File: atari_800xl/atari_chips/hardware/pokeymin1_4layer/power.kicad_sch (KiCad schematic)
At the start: 10 parts

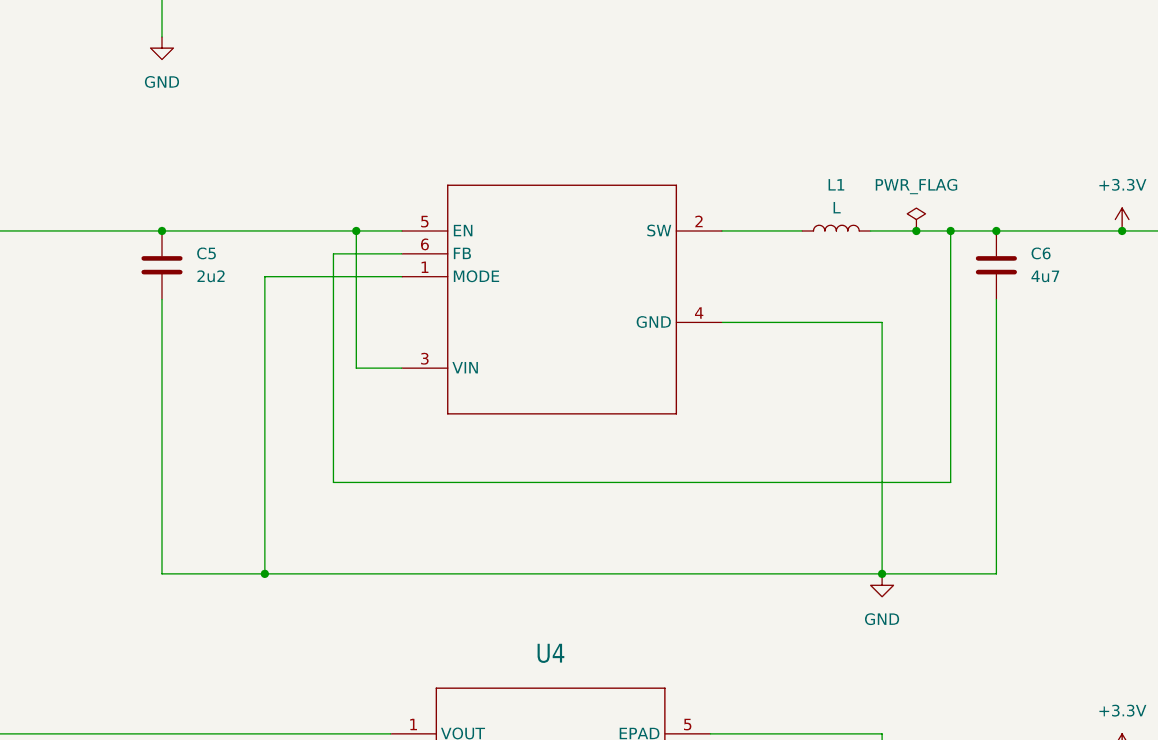
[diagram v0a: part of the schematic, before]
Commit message: Change regulator to a linear one that works with the io pin protection scheme
git-svn-id: svn+ssh://192.168.0.3/home/svnfpga/repo/trunk@1479 d6161ac3-aae1-4d52-9b05-ea9ac36b53d3
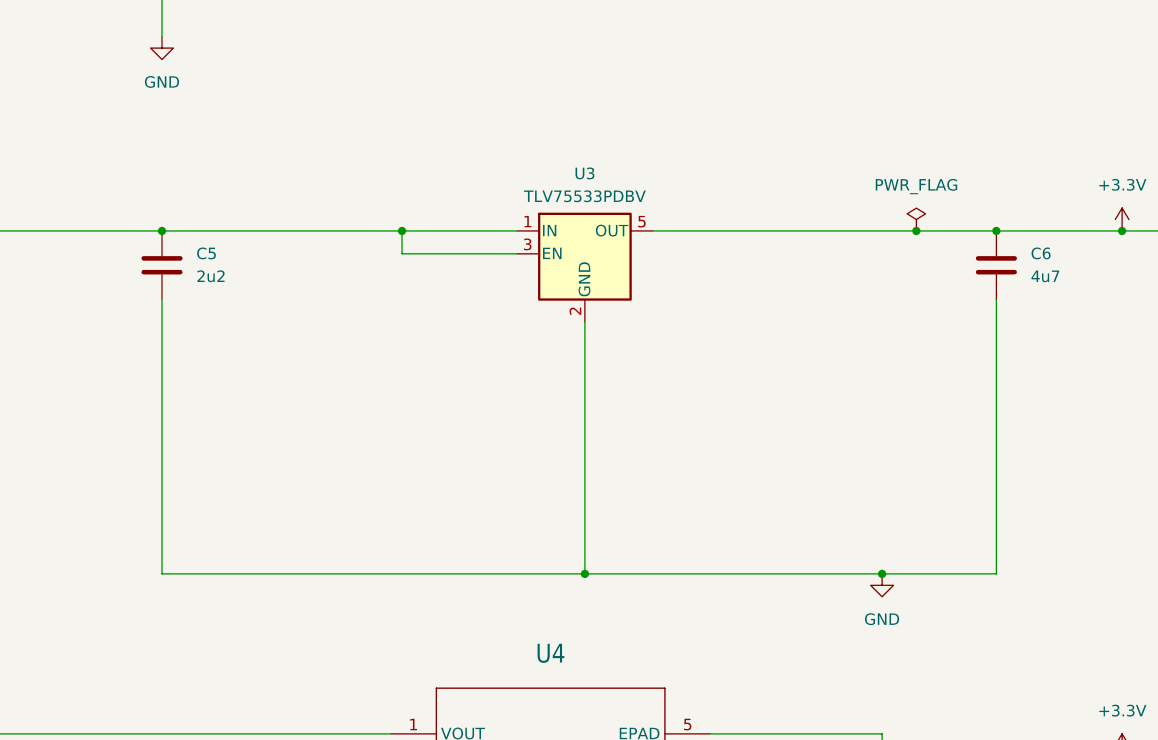
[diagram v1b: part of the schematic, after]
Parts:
- removed L1: L, Inductor_SMD:L_1008_2520Metric_Pad1.43x2.20mm_HandSolder, symbol Device:L
- removed U3: ~, max10:DRY6, symbol max10u169:TPS62237DRYR
- added U3: TLV75533PDBV, Package_TO_SOT_SMD:SOT-23-5, symbol Regulator_Linear:TLV75533PDBV
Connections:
- net +3.3V: now also U3.5 (OUT)
- net +5V: now also U3.1 (IN), U3.3 (EN)
- net GND: now also U3.2 (GND)
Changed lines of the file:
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@@
 	(paper "A4")
+	(junction
+		(at 83.82 60.96)
+		(diameter 0)
+		(color 0 0 0 0)
+	)
 	(junction
 		(at 57.15 60.96)
@@
 	)
 	(junction
-		(at 68.58 99.06)
-		(diameter 0)
-		(color 0 0 0 0)
-	)
-	(junction
 		(at 50.8 31.75)
 		(diameter 0)
@@
 	)
 	(junction
-		(at 144.78 60.96)
-		(diameter 0)
-		(color 0 0 0 0)
-	)
-	(junction
 		(at 62.23 31.75)
 		(diameter 0)
@@
 	)
 	(junction
-		(at 78.74 60.96)
+		(at 104.14 99.06)
 		(diameter 0)
 		(color 0 0 0 0)
@@
 	(wire
 		(pts
-			(xy 78.74 76.2) (xy 78.74 60.96)
-		)
-		(stroke
-			(width 0)
-			(type default)
-		)
-	)
-	(wire
-		(pts
-			(xy 137.16 99.06) (xy 137.16 71.12)
-		)
-		(stroke
-			(width 0)
-			(type default)
-		)
-	)
-	(wire
-		(pts
 			(xy 50.8 31.75) (xy 57.15 31.75)
 		)
@@
 	(wire
 		(pts
-			(xy 140.97 60.96) (xy 144.78 60.96)
+			(xy 140.97 60.96) (xy 149.86 60.96)
 		)
 		(stroke
@@
 	(wire
 		(pts
-			(xy 76.2 63.5) (xy 83.82 63.5)
-		)
-		(stroke
-			(width 0)
-			(type default)
-		)
-	)
-	(wire
-		(pts
-			(xy 68.58 66.04) (xy 68.58 99.06)
-		)
-		(stroke
-			(width 0)
-			(type default)
-		)
-	)
-	(wire
-		(pts
 			(xy 57.15 68.58) (xy 57.15 99.06)
 		)
@@
 	(wire
 		(pts
-			(xy 83.82 66.04) (xy 68.58 66.04)
+			(xy 96.52 63.5) (xy 83.82 63.5)
+		)
+		(stroke
+			(width 0)
+			(type default)
+		)
+	)
+	(wire
+		(pts
+			(xy 111.76 60.96) (xy 140.97 60.96)
 		)
 		(stroke
@@
 	(wire
 		(pts
-			(xy 135.89 60.96) (xy 140.97 60.96)
-		)
-		(stroke
-			(width 0)
-			(type default)
-		)
-	)
-	(wire
-		(pts
-			(xy 83.82 76.2) (xy 78.74 76.2)
-		)
-		(stroke
-			(width 0)
-			(type default)
-		)
-	)
-	(wire
-		(pts
 			(xy 118.11 121.92) (xy 123.19 121.92)
 		)
@@
 	(wire
 		(pts
-			(xy 119.38 60.96) (xy 128.27 60.96)
+			(xy 104.14 71.12) (xy 104.14 99.06)
 		)
 		(stroke
@@
 	(wire
 		(pts
-			(xy 78.74 60.96) (xy 83.82 60.96)
-		)
-		(stroke
-			(width 0)
-			(type default)
-		)
-	)
-	(wire
-		(pts
 			(xy 34.29 60.96) (xy 57.15 60.96)
 		)
@@
 	(wire
 		(pts
+			(xy 104.14 99.06) (xy 137.16 99.06)
+		)
+		(stroke
+			(width 0)
+			(type default)
+		)
+	)
+	(wire
+		(pts
 			(xy 123.19 121.92) (xy 123.19 119.38)
 		)
@@
 	(wire
 		(pts
+			(xy 83.82 60.96) (xy 96.52 60.96)
+		)
+		(stroke
+			(width 0)
+			(type default)
+		)
+	)
+	(wire
+		(pts
 			(xy 149.86 68.58) (xy 149.86 99.06)
 		)
@@
 	(wire
 		(pts
-			(xy 144.78 60.96) (xy 149.86 60.96)
-		)
-		(stroke
-			(width 0)
-			(type default)
-		)
-	)
-	(wire
-		(pts
 			(xy 62.23 21.59) (xy 62.23 24.13)
 		)
@@
 	(wire
 		(pts
-			(xy 144.78 88.9) (xy 76.2 88.9)
-		)
-		(stroke
-			(width 0)
-			(type default)
-		)
-	)
-	(wire
-		(pts
-			(xy 76.2 88.9) (xy 76.2 63.5)
+			(xy 83.82 63.5) (xy 83.82 60.96)
 		)
 		(stroke
@@
 	(wire
 		(pts
-			(xy 68.58 99.06) (xy 137.16 99.06)
+			(xy 57.15 99.06) (xy 104.14 99.06)
 		)
 		(stroke
@@
 	(wire
 		(pts
-			(xy 144.78 60.96) (xy 144.78 88.9)
-		)
-		(stroke
-			(width 0)
-			(type default)
-		)
-	)
-	(wire
-		(pts
-			(xy 57.15 99.06) (xy 68.58 99.06)
-		)
-		(stroke
-			(width 0)
-			(type default)
-		)
-	)
-	(wire
-		(pts
 			(xy 57.15 31.75) (xy 57.15 39.37)
 		)
@@
 	(wire
 		(pts
-			(xy 57.15 60.96) (xy 78.74 60.96)
-		)
-		(stroke
-			(width 0)
-			(type default)
-		)
-	)
-	(wire
-		(pts
-			(xy 137.16 71.12) (xy 119.38 71.12)
+			(xy 57.15 60.96) (xy 83.82 60.96)
 		)
 		(stroke
@@
 	)
 	(symbol
+		(lib_id "Regulator_Linear:TLV75533PDBV")
+		(at 104.14 63.5 0)
+		(unit 1)
+		(exclude_from_sim no)
+		(in_bom yes)
+		(on_board yes)
+		(dnp no)
+		(fields_autoplaced yes)
+		(property "Reference" "U3"
+			(at 104.14 54.61 0)
+			(effects
+				(font
+					(size 1.27 1.27)
+				)
+			)
+		)
+		(property "Value" "TLV75533PDBV"
+			(at 104.14 57.15 0)
+			(effects
+				(font
+					(size 1.27 1.27)
+				)
+			)
+		)
+		(property "Footprint" "Package_TO_SOT_SMD:SOT-23-5"
+			(at 104.14 55.245 0)
+			(effects
+				(font
+					(size 1.27 1.27)
+					(italic yes)
+				)
+				(hide yes)
+			)
+		)
+		(property "Datasheet" "http://www.ti.com/lit/ds/symlink/tlv755p.pdf"
+			(at 104.14 62.23 0)
+			(effects
+				(font
+					(size 1.27 1.27)
+				)
+				(hide yes)
+			)
+		)
+		(property "Description" "500mA Low Dropout Voltage Regulator, Fixed Output 3.3V, SOT-23-5"
+			(at 104.14 63.5 0)
+			(effects
+				(font
+					(size 1.27 1.27)
+				)
+				(hide yes)
+			)
+		)
+		(pin "5"
+		)
+		(pin "4"
+		)
+		(pin "1"
+		)
+		(pin "3"
+		)
+		(pin "2"
+		)
+		(instances
+			(project ""
+				(path "/f8f92944-710a-49a0-a698-f840e5f20e15/b3c63cf3-5aec-4ac7-b511-941f39b58d95"
+					(reference "U3")
+					(unit 1)
+				)
+			)
+		)
+	)
+	(symbol
 		(lib_id "power:PWR_FLAG")
 		(at 140.97 60.96 0)
@@
 					(unit 1)
 				)
-			)
-		)
-	)
-	(symbol
-		(lib_id "Device:L")
-		(at 132.08 60.96 90)
-		(unit 1)
-		(exclude_from_sim no)
-		(in_bom yes)
-		(on_board yes)
-		(dnp no)
-		(fields_autoplaced yes)
-		(property "Reference" "L1"
-			(at 132.08 55.88 90)
-			(effects
-				(font
-					(size 1.27 1.27)
-				)
-			)
-		)
-		(property "Value" "L"
-			(at 132.08 58.42 90)
-			(effects
-				(font
-					(size 1.27 1.27)
-				)
-			)
-		)
-		(property "Footprint" "Inductor_SMD:L_1008_2520Metric_Pad1.43x2.20mm_HandSolder"
-			(at 132.08 60.96 0)
-			(effects
-				(font
-					(size 1.27 1.27)
-				)
-				(hide yes)
-			)
-		)
-		(property "Datasheet" "~"
-			(at 132.08 60.96 0)
-			(effects
-				(font
-					(size 1.27 1.27)
-				)
-				(hide yes)
-			)
-		)
-		(property "Description" "Inductor"
-			(at 132.08 60.96 0)
-			(effects
-				(font
-					(size 1.27 1.27)
-				)
-				(hide yes)
-			)
-		)
-		(pin "2"
-		)
-		(pin "1"
-		)
-		(instances
-			(project ""
-				(path "/f8f92944-710a-49a0-a698-f840e5f20e15/b3c63cf3-5aec-4ac7-b511-941f39b58d95"
-					(reference "L1")
-					(unit 1)
-				)
-			)
-		)
-	)
-	(symbol
-		(lib_id "max10u169:TPS62237DRYR")
-		(at 81.28 60.96 0)
-		(unit 1)
-		(exclude_from_sim no)
-		(in_bom yes)
-		(on_board yes)
-		(dnp no)
-		(fields_autoplaced yes)
-		(property "Reference" "U3"
-			(at 96.8756 51.8414 0)
-			(effects
-				(font
-					(size 2.0828 1.7703)
-				)
-				(justify left bottom)
-				(hide yes)
-			)
-		)
-		(property "Value" "~"
-			(at 96.2406 54.3814 0)
-			(effects
-				(font
-					(size 2.0828 1.7703)
-				)
-				(justify left bottom)
-				(hide yes)
-			)
-		)
-		(property "Footprint" "max10:DRY6"
-			(at 81.28 60.96 0)
-			(effects
-				(font
-					(size 1.27 1.27)
-				)
-				(hide yes)
-			)
-		)
-		(property "Datasheet" ""
-			(at 81.28 60.96 0)
-			(effects
-				(font
-					(size 1.27 1.27)
-				)
-				(hide yes)
-			)
-		)
-		(property "Description" ""
-			(at 81.28 60.96 0)
-			(effects
-				(font
-					(size 1.27 1.27)
-				)
-				(hide yes)
-			)
-		)
-		(pin "1"
-		)
-		(pin "5"
-		)
-		(pin "3"
-		)
-		(pin "6"
-		)
-		(pin "4"
-		)
-		(pin "2"
-		)
-		(instances
-			(project ""
-				(path "/f8f92944-710a-49a0-a698-f840e5f20e15/b3c63cf3-5aec-4ac7-b511-941f39b58d95"
-					(reference "U3")
-					(unit 1)
-				)
